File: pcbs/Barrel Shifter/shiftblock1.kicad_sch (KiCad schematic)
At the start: 1 part, among them U201 74HC138

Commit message: Second row
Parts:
- removed U201: 74HC138, Package_DIP:DIP-16_W7.62mm_Socket, symbol 74xx:74HC138
- added U301: 74HC138, Package_DIP:DIP-16_W7.62mm_Socket, symbol 74xx:74HC138
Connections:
- net +5V: now also U301.16 (VCC)
- net GND: now also U301.8 (GND)
- new net ~{Y10}: U301.13 (~{Y2})
- new net ~{Y11}: U301.12 (~{Y3})
- new net ~{Y12}: U301.11 (~{Y4})
- new net ~{Y13}: U301.10 (~{Y5})
- new net ~{Y14}: U301.9 (~{Y6})
- new net ~{Y15}: U301.7 (~{Y7})
- new net ~{Y8}: U301.15 (~{Y0})
- new net ~{Y9}: U301.14 (~{Y1})
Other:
- removed sheet Shifter 0
- removed sheet Shifter 1
- removed sheet Shifter 2
- removed sheet Shifter 3
- removed sheet Shifter 4
- removed sheet Shifter 5
- removed sheet Shifter 6
- removed sheet Shifter 7
- added sheet Shifter 10 (shifter.kicad_sch)
- added sheet Shifter 11 (shifter.kicad_sch)
- added sheet Shifter 12 (shifter.kicad_sch)
- added sheet Shifter 13 (shifter.kicad_sch)
- added sheet Shifter 14 (shifter.kicad_sch)
- added sheet Shifter 15 (shifter.kicad_sch)
- added sheet Shifter 8 (shifter.kicad_sch)
- added sheet Shifter 9 (shifter.kicad_sch)

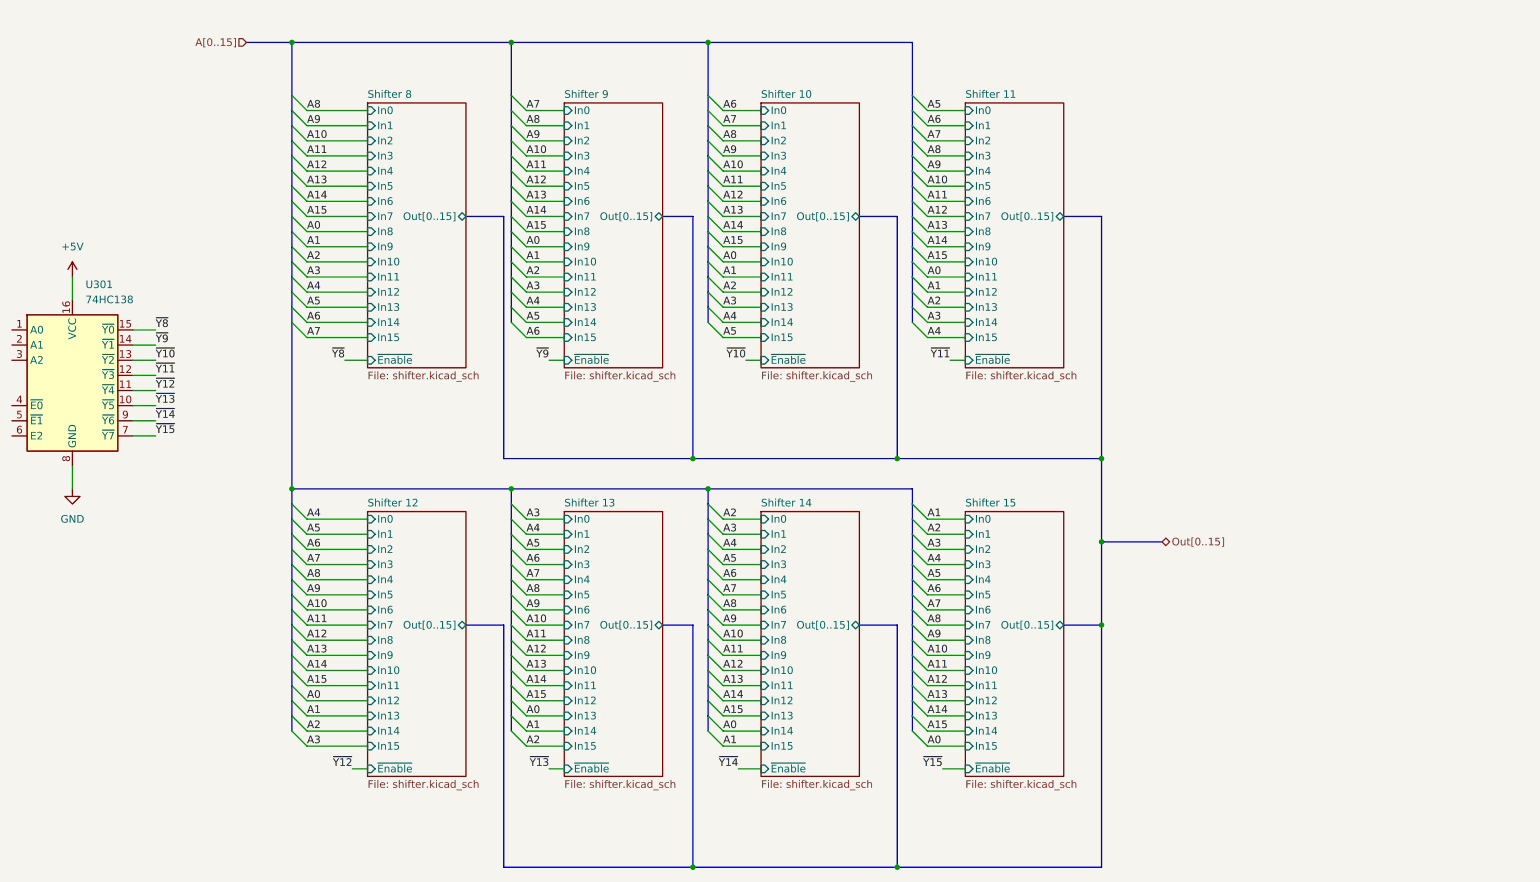
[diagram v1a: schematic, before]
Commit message: Starting to tidy up the LEDs
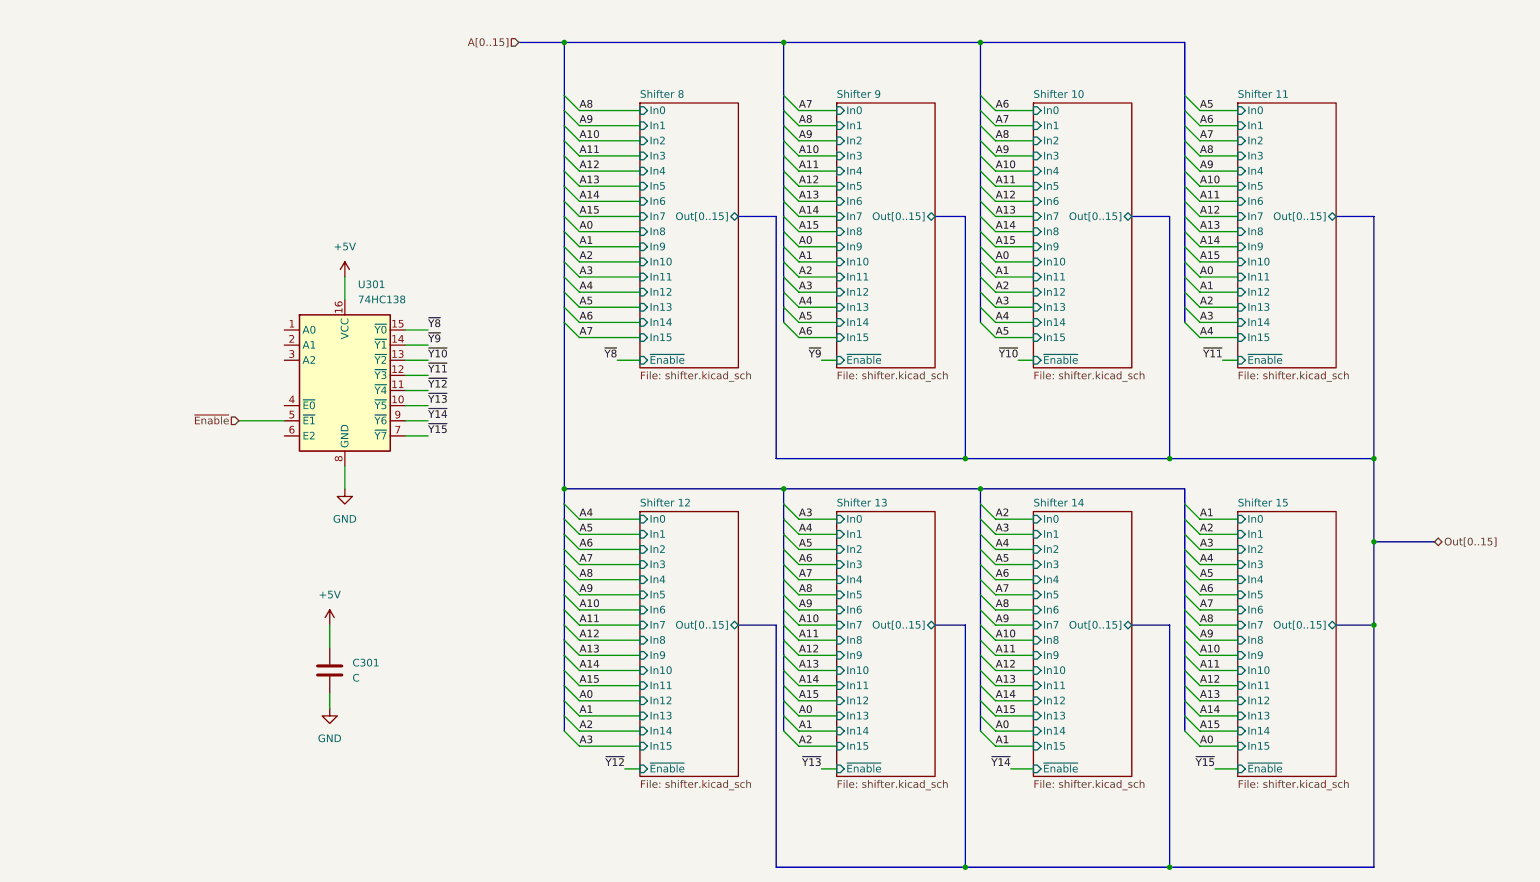
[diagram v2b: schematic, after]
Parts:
- added C301: C, Capacitor_SMD:C_0603_1608Metric, symbol Device:C
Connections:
- net +5V: now also C301.1
- net GND: now also C301.2
- net ~{Enable}: now reaches U301.5 (~{E1})
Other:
- moved on the sheet: U301
